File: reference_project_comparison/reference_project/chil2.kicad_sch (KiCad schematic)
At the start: 2 parts

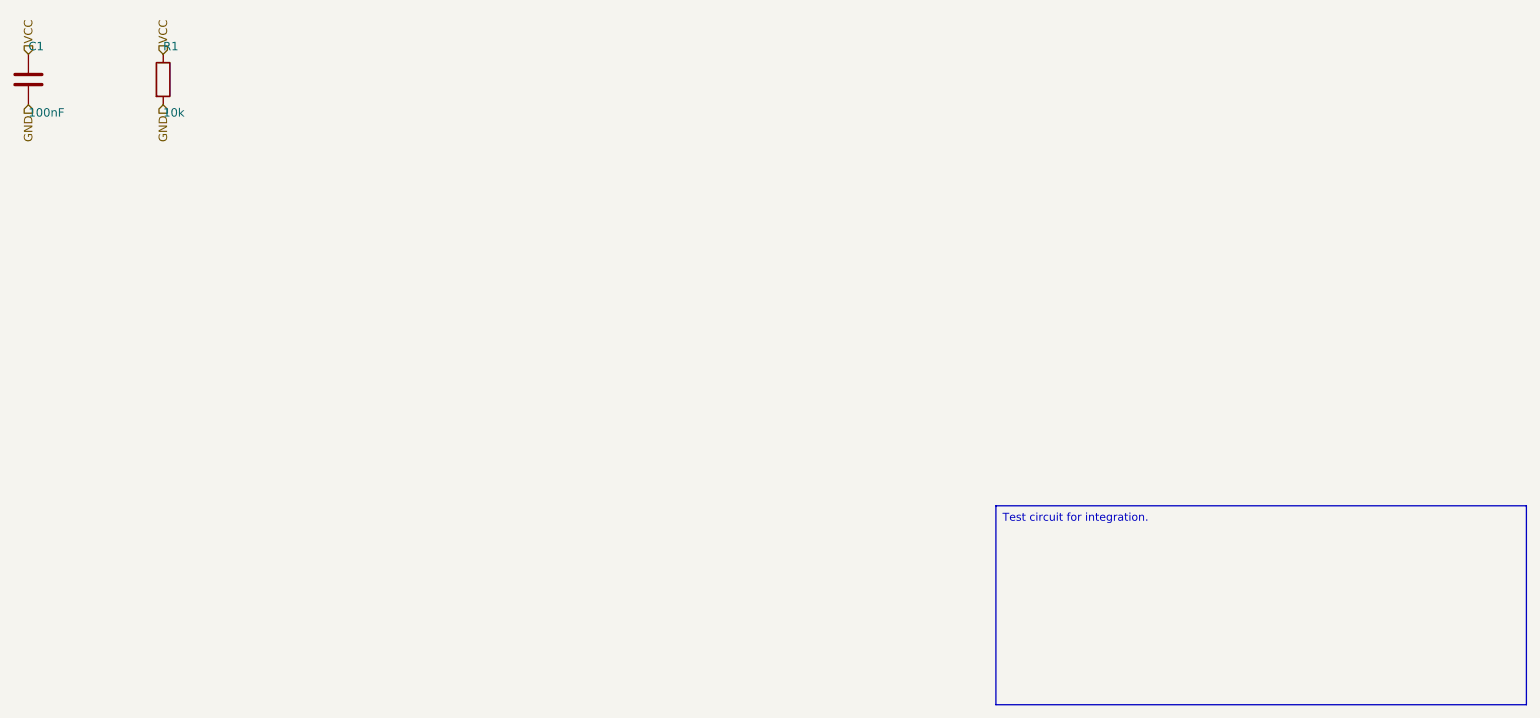
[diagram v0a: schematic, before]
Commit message: remove unused files and add reference project for debuggin help
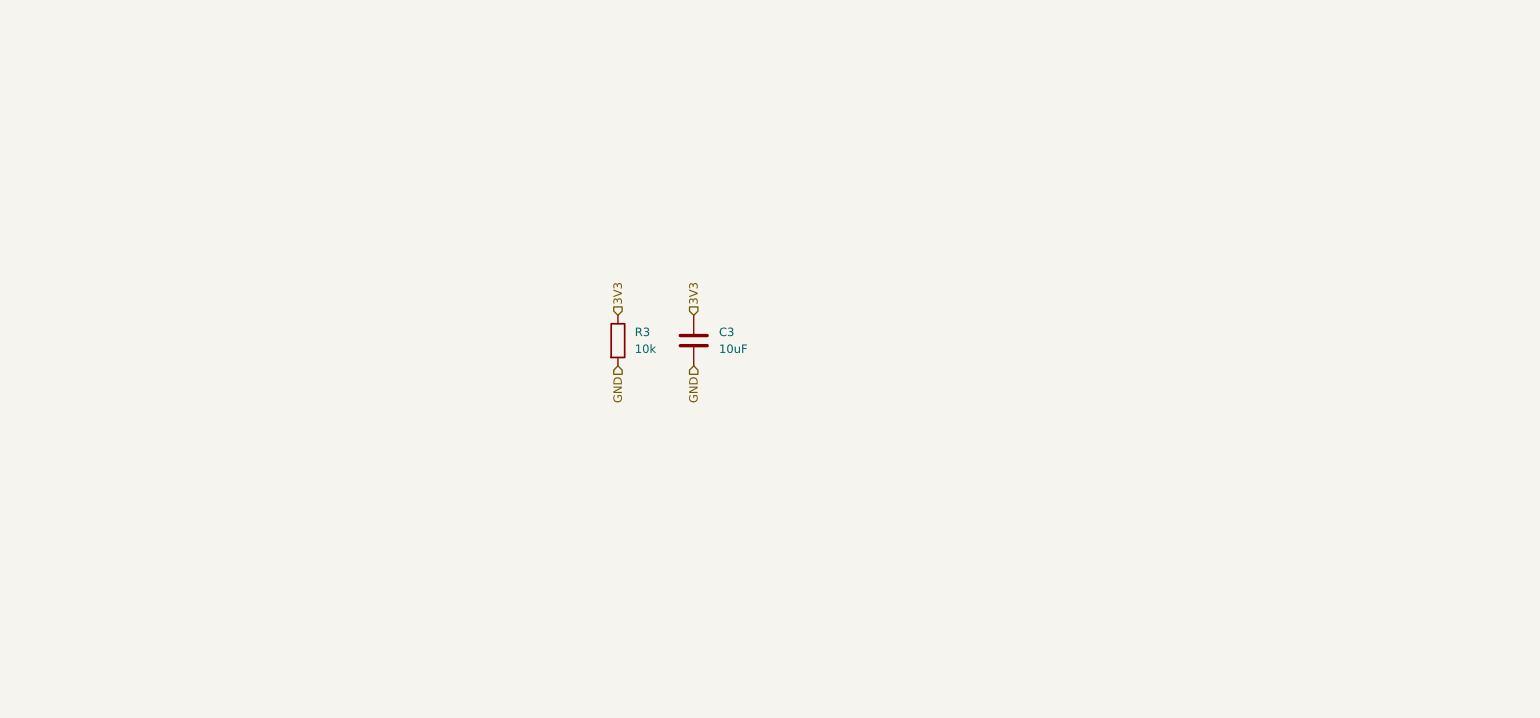
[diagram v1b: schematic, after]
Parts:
- removed C1: 100nF, symbol Device:C
- removed R1: 10k, symbol Device:R
- added C3: 10uF, Capacitor_SMD:C_0603_1608Metric, symbol Device:C
- added R3: 10k, Resistor_SMD:R_0603_1608Metric, symbol Device:R
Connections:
- net GND: now also C3.2, R3.2
- new net 3V3: C3.1, R3.1
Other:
- company: Circuit-Synth -> (none)
- title: test_basic -> (none)
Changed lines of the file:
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@@
 (kicad_sch
 	(version 20250114)
-	(generator "circuit_synth")
+	(generator "eeschema")
 	(generator_version "9.0")
 	(paper "A4")
-	(title_block
-		(title test_basic)
-		(date 2025-08-06)
-		(company Circuit-Synth)
+	(hierarchical_label "GND"
+		(shape input)
+		(at 127 88.9 270)
+		(effects
+			(font
+				(size 1.27 1.27)
+			)
+			(justify right)
+		)
+	)
+	(hierarchical_label "GND"
+		(shape input)
+		(at 138.43 88.9 270)
+		(effects
+			(font
+				(size 1.27 1.27)
+			)
+			(justify right)
+		)
+	)
+	(hierarchical_label "3V3"
+		(shape input)
+		(at 138.43 81.28 90)
+		(effects
+			(font
+				(size 1.27 1.27)
+			)
+			(justify left)
+		)
+	)
+	(hierarchical_label "3V3"
+		(shape input)
+		(at 127 81.28 90)
+		(effects
+			(font
+				(size 1.27 1.27)
+			)
+			(justify left)
+		)
 	)
 	(symbol
 		(lib_id "Device:R")
-		(at 58.42 45.72 0)
+		(at 127 85.09 0)
 		(unit 1)
 		(exclude_from_sim no)
@@
 		(dnp no)
 		(fields_autoplaced yes)
-		(property "Reference" "R1"
-			(at 58.42 40.72 0)
+		(property "Reference" "R3"
+			(at 129.54 83.8199 0)
 			(effects
 				(font
@@
 		)
 		(property "Value" "10k"
-			(at 58.42 50.72 0)
+			(at 129.54 86.3599 0)
 			(effects
 				(font
@@
 			)
 		)
+		(property "Footprint" "Resistor_SMD:R_0603_1608Metric"
+			(at 125.222 85.09 90)
+			(effects
+				(font
+					(size 1.27 1.27)
+				)
+				(hide yes)
+			)
+		)
+		(property "Datasheet" "~"
+			(at 127 85.09 0)
+			(effects
+				(font
+					(size 1.27 1.27)
+				)
+				(hide yes)
+			)
+		)
+		(property "Description" "Resistor"
+			(at 127 85.09 0)
+			(effects
+				(font
+					(size 1.27 1.27)
+				)
+				(hide yes)
+			)
+		)
+		(pin "1"
+		)
+		(pin "2"
+		)
 		(instances
-			(project ""
-				(path "/13669d76-745f-40f5-b839-01e30f56c31a"
-					(reference "R1")
+			(project "reference_project"
+				(path "/02d7f802-483d-49cf-8375-f5d7aced54aa/96832371-9fbd-4f17-910c-abdc4f672a36/b63cccbe-076a-4d64-844f-4217dcdbd372"
+					(reference "R3")
 					(unit 1)
 				)
@@
 	(symbol
 		(lib_id "Device:C")
-		(at 38.1 45.72 0)
+		(at 138.43 85.09 0)
 		(unit 1)
 		(exclude_from_sim no)
@@
 		(dnp no)
 		(fields_autoplaced yes)
-		(property "Reference" "C1"
-			(at 38.1 40.72 0)
+		(property "Reference" "C3"
+			(at 142.24 83.8199 0)
 			(effects
 				(font
@@
 			)
 		)
-		(property "Value" "100nF"
-			(at 38.1 50.72 0)
+		(property "Value" "10uF"
+			(at 142.24 86.3599 0)
 			(effects
 				(font
@@
 			)
 		)
+		(property "Footprint" "Capacitor_SMD:C_0603_1608Metric"
+			(at 139.3952 88.9 0)
+			(effects
+				(font
+					(size 1.27 1.27)
+				)
+				(hide yes)
+			)
+		)
+		(property "Datasheet" "~"
+			(at 138.43 85.09 0)
+			(effects
+				(font
+					(size 1.27 1.27)
+				)
+				(hide yes)
+			)
+		)
+		(property "Description" "Unpolarized capacitor"
+			(at 138.43 85.09 0)
+			(effects
+				(font
+					(size 1.27 1.27)
+				)
+				(hide yes)
+			)
+		)
+		(pin "1"
+		)
+		(pin "2"
+		)
 		(instances
-			(project ""
-				(path "/13669d76-745f-40f5-b839-01e30f56c31a"
-					(reference "C1")
+			(project "reference_project"
+				(path "/02d7f802-483d-49cf-8375-f5d7aced54aa/96832371-9fbd-4f17-910c-abdc4f672a36/b63cccbe-076a-4d64-844f-4217dcdbd372"
+					(reference "C3")
 					(unit 1)
 				)
@@
 		)
 	)
-	(hierarchical_label
-		VCC
-		(shape input)
-		(at 58.42 41.91 90)
-		(effects
-			(font
-				(size 1.27 1.27)
-			)
-			(justify left)
-		)
-	)
-	(hierarchical_label
-		VCC
-		(shape input)
-		(at 38.1 41.91 90)
-		(effects
-			(font
-				(size 1.27 1.27)
-			)
-			(justify left)
-		)
-	)
-	(hierarchical_label
-		GND
-		(shape input)
-		(at 58.42 49.53 270)
-		(effects
-			(font
-				(size 1.27 1.27)
-			)
-			(justify right)
-		)
-	)
-	(hierarchical_label
-		GND
-		(shape input)
-		(at 38.1 49.53 270)
-		(effects
-			(font
-				(size 1.27 1.27)
-			)
-			(justify right)
-		)
-	)
-	(text_box
-		"Test circuit for integration."
-		(exclude_from_sim yes)
-		(at 184.0 110.0 0)
-		(size 80.0 30.0)
-		(margins
-			1.0
-			1.0
-			1.0
-			1.0
-		)
-		(stroke
-			(width 0.1)
-			(type solid)
-		)
-		(fill
-			(type color)
-			(color
-				255
-				255
-				224
-				1
-			)
-		)
-		(effects
-			(font
-				(size 1.2 1.2)
-				(thickness 0.254)
-			)
-			(justify left top)
-		)
-	)
-	(sheet_instances
-		(path "/13669d76-745f-40f5-b839-01e30f56c31a"
-			(page "1")
-		)
-	)
-	(embedded_fonts no)
 )
